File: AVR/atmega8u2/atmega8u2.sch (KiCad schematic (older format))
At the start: 11 parts

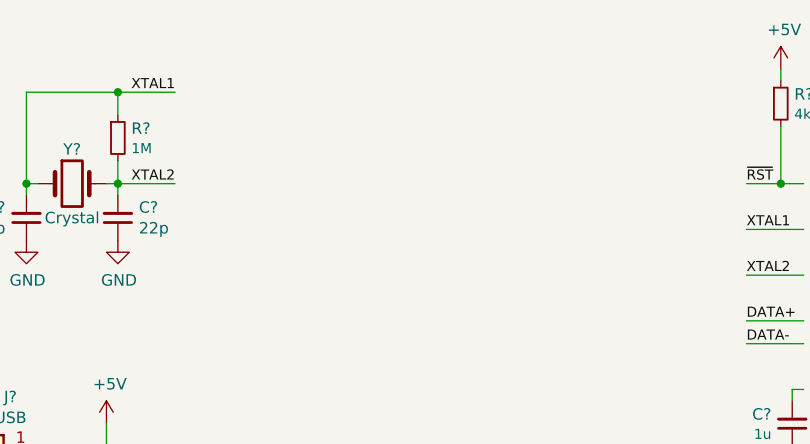
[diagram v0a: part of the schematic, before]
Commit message: Improving AVR templates
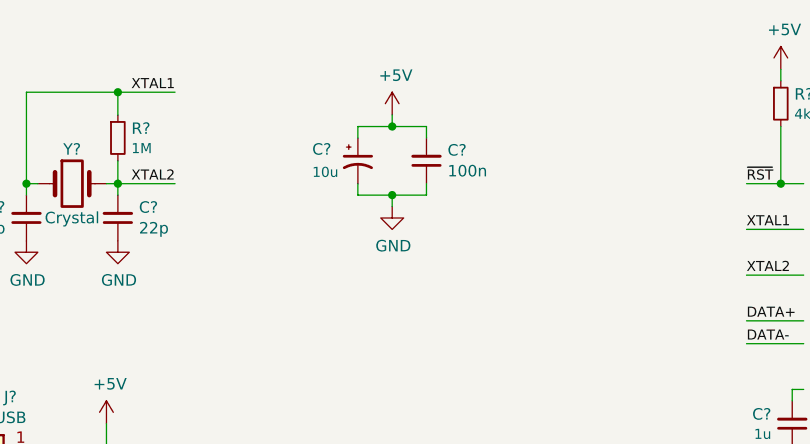
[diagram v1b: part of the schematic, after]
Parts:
- added C?: 100n, symbol Device:C_Small
- added C?: 10u, symbol Device:CP1_Small
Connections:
- wire segments 52 -> 62
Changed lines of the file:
@@
 EESchema Schematic File Version 4
-LIBS:atmega8-cache
+LIBS:atmega8u2-cache
 EELAYER 26 0
 EELAYER END
@@
 Wire Wire Line
 	2150 3900 2400 3900
+$Comp
+L Device:C_Small C?
+U 1 1 5B8596A1
+P 3600 2450
+F 0 "C?" H 3508 2404 50  0000 R CNN
+F 1 "100n" H 3508 2495 50  0000 R CNN
+F 2 "" H 3600 2450 50  0001 C CNN
+F 3 "~" H 3600 2450 50  0001 C CNN
+	1    3600 2450
+	-1   0    0    1
+$EndComp
+$Comp
+L power:GND #PWR?
+U 1 1 5B8596EA
+P 3450 2650
+F 0 "#PWR?" H 3450 2400 50  0001 C CNN
+F 1 "GND" H 3455 2477 50  0000 C CNN
+F 2 "" H 3450 2650 50  0001 C CNN
+F 3 "" H 3450 2650 50  0001 C CNN
+	1    3450 2650
+	1    0    0    -1
+$EndComp
+$Comp
+L Device:CP1_Small C?
+U 1 1 5B859730
+P 3300 2450
+F 0 "C?" H 3100 2500 50  0000 L CNN
+F 1 "10u" H 3100 2400 44  0000 L CNN
+F 2 "" H 3300 2450 50  0001 C CNN
+F 3 "~" H 3300 2450 50  0001 C CNN
+	1    3300 2450
+	1    0    0    -1
+$EndComp
+Wire Wire Line
+	3300 2550 3300 2600
+Wire Wire Line
+	3300 2600 3450 2600
+Wire Wire Line
+	3600 2600 3600 2550
+Wire Wire Line
+	3450 2600 3450 2650
+Connection ~ 3450 2600
+Wire Wire Line
+	3450 2600 3600 2600
+Wire Wire Line
+	3300 2350 3300 2300
+Wire Wire Line
+	3300 2300 3450 2300
+Wire Wire Line
+	3600 2300 3600 2350
+$Comp
+L power:+5V #PWR?
+U 1 1 5B85C176
+P 3450 2250
+F 0 "#PWR?" H 3450 2100 50  0001 C CNN
+F 1 "+5V" H 3465 2423 50  0000 C CNN
+F 2 "" H 3450 2250 50  0001 C CNN
+F 3 "" H 3450 2250 50  0001 C CNN
+	1    3450 2250
+	1    0    0    -1
+$EndComp
+Wire Wire Line
+	3450 2250 3450 2300
+Connection ~ 3450 2300
+Wire Wire Line
+	3450 2300 3600 2300
 $EndSCHEMATC

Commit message: Update to KiCad 5.1.7
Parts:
- U?: symbol MCU_Microchip_ATmega:ATmega8U2-AU -> atmega8u2-rescue:ATmega8U2-AU-MCU_Microchip_ATmega
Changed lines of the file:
@@
 EESchema Schematic File Version 4
-LIBS:atmega8u2-cache
-EELAYER 26 0
+EELAYER 30 0
 EELAYER END
 $Descr A4 11693 8268
@@
 	2300 5700 2300 5900
 $Comp
-L MCU_Microchip_ATmega:ATmega8U2-AU U?
+L atmega8u2-rescue:ATmega8U2-AU-MCU_Microchip_ATmega U?
 U 1 1 5B841C83
 P 5950 3650
